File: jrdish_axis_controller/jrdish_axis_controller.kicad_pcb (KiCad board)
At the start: 4 copper layers, 100 x 100 mm, 234 parts, among them CN1 KF2EDGR-2.54-9P, CN10 KF2EDGR-2.54-2P, CN11 KF2EDGR-2.54-3P, CN12 KF2EDGR-2.54-9P, CN13 KF2EDGR-2.54-6P, CN14 KF2EDGR-2.54-6P, CN2 KF2EDGR-2.54-6P, CN3 KF2EDGR-2.54-4P, CN4 KF2EDGR-2.54-4P, CN5 KF2EDGR-2.54-4P, CN7 SM04B-SRSS-TB (LF)(SN), CN8 SM04B-SRSS-TB (LF)(SN), CN9 KF2EDGR-2.54-2P, J1 Conn_ARM_SWD_TagConnect_TC2030, M1 MountingHole_2.7mm_M2.5_ISO14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, Q1 AO3407A, Q2 AO3400A, Q3 BSS138, Q4 AO3407A, Q5 BSS138, Q6 BSS138, Q7 BSS138, Q8 BSS138, SW1 DSHP04TSGER, SW2 SS-12F49-G050, U1 STM32G474RET6, U2 ISOW1432BDFMR, U3 ISOW1432BDFMR, U4 MP2322GQH-Z, U5 LTC4311ISC6#TRPBF, U6 LM75BIMX-3/NOPB, U7 W25Q32JVSSIQ_C179173, X1 NX2016SA-16MHZ-EXS00A-CS07826

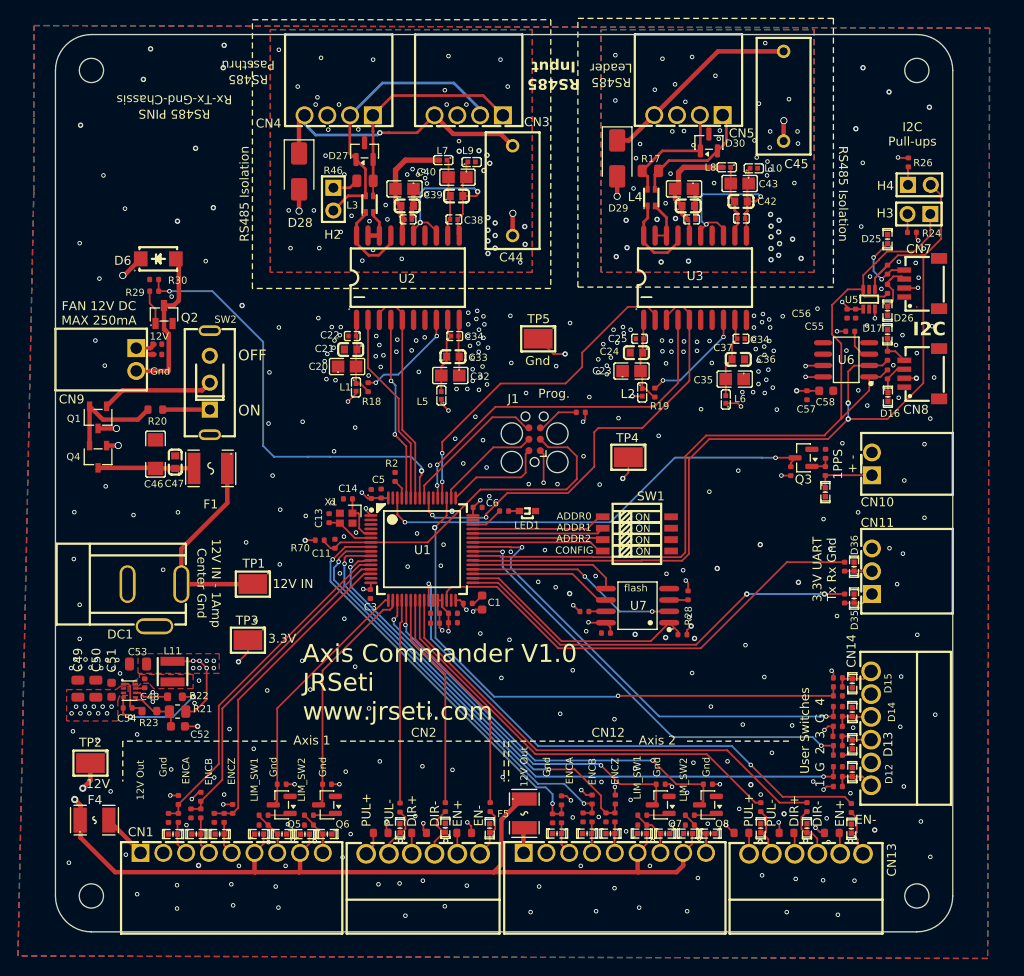
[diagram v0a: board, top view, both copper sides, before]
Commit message: Updates for replacing 10k resistors and encoder RC.
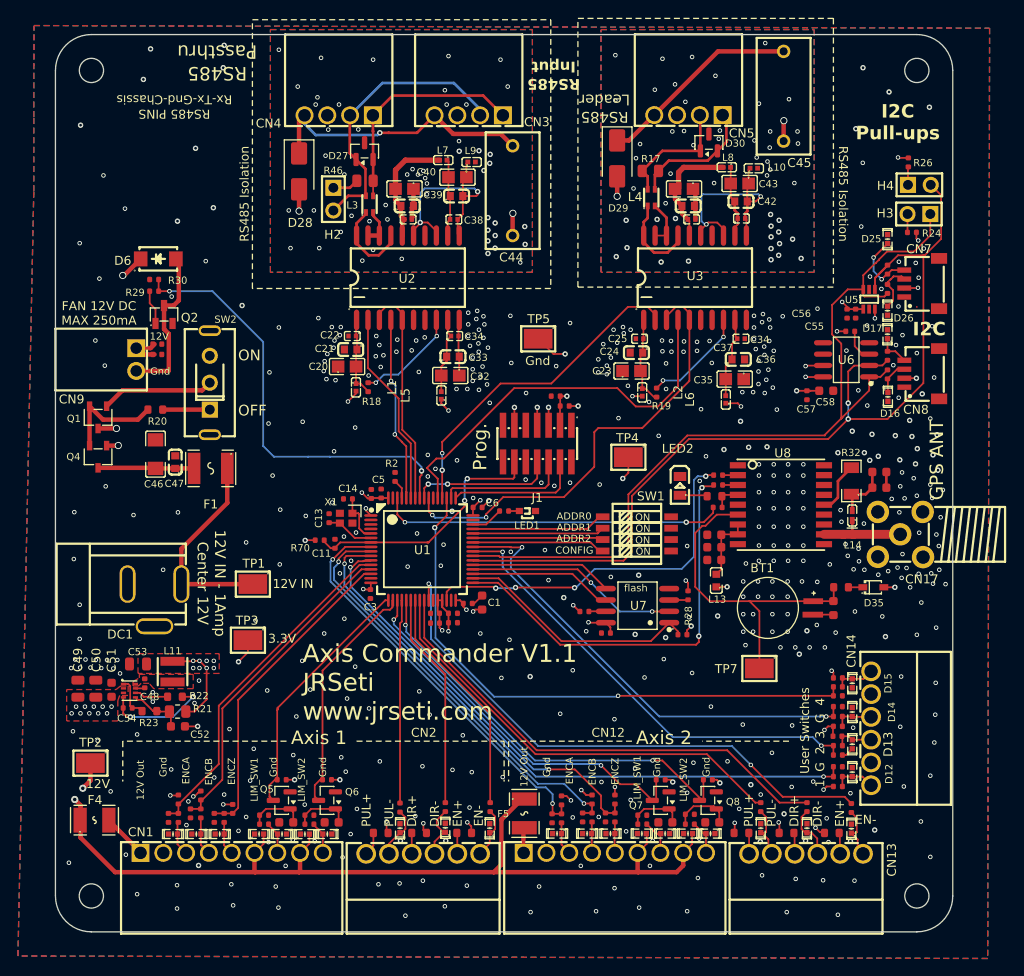
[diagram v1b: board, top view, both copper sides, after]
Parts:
- removed CN10: KF2EDGR-2.54-2P, MyParts:CONN-TH_P2.54_KF2EDGR-2.54-2P
- removed CN11: KF2EDGR-2.54-3P, MyParts:CONN-TH_3P-P2.54_KF2EDGR-2.54-3P
- removed D24, D36: TPESD0402G05V, MyParts:D0402-BI
- removed Q3: BSS138, Package_TO_SOT_SMD:SOT-23
- removed R63: 10kΩ, PCM_JLCPCB:R_0402
- added BT1: MS621FE-FL11E, MyParts:BAT_MS621FE-FL11E, F.Cu at (194.8, 96.5)
- added C12: 10nF, PCM_JLCPCB:C_0603, F.Cu at (207.2, 81.3)
- added C18: 100nF, PCM_JLCPCB:C_0402, F.Cu at (171.2, 72.9)
- added C19: 10uF, PCM_JLCPCB:C_0603, F.Cu at (188.8, 91.2)
- added C62: 100nF, PCM_JLCPCB:C_0603, F.Cu at (188.8, 89.7)
- added C63: 1uF, PCM_JLCPCB:C_0603, F.Cu at (202.1, 96.5)
- added C64: 100nF, PCM_JLCPCB:C_0603, F.Cu at (188.8, 88.3)
- added C65: 47pF, PCM_JLCPCB:C_0603, F.Cu at (207.2, 83.1)
- added C66: 10nF, PCM_JLCPCB:C_0603, F.Cu at (141.1, 120.4)
- added C70: 10nF, PCM_JLCPCB:C_0603, F.Cu at (146.2, 120.4)
- added C71: 10nF, PCM_JLCPCB:C_0603, F.Cu at (183.4, 120.4)
- added C76: 10nF, PCM_JLCPCB:C_0603, F.Cu at (188.6, 120.4)
- added CN17: SMA-KWE_C7498154, MyParts:SMA-TH_SMA-KWE_C7498154, F.Cu at (209.6, 88.3)
- added L13: BLM18AG601SN1D, MyParts:L0603, F.Cu at (189.1, 93.5)
- added L14: LQG15HS27NJ02D, MyParts:L0402-RD, F.Cu at (204.2, 86.2)
- added LED2: XL-0805QBC, MyParts:LED0805-R-RD, F.Cu at (185.0, 82.9)
- added R1: 1kΩ, PCM_JLCPCB:R_0402, F.Cu at (189.2, 85.3)
- added R12: 1kΩ, PCM_JLCPCB:R_0603, F.Cu at (188.8, 84.0)
- added TP7: RH-5016, MyParts:TESTPOINT-SMD_L3.0-W2.0, F.Cu at (193.8, 103.2)
- added U8: MAX-M10S-00B, MyParts:SMD-18_L10.1-W9.7-P1.10-TL_SKG09F, F.Cu at (196.2, 85.0)
- C15, C16, C17, C67, C68, C69: value 100nF -> 1nF
- D35: value TPESD0402G05V -> 1N4148WS T4; footprint MyParts:D0402-BI -> MyParts:SOD-323_L1.8-W1.3-LS2.5-RD
- J1: value Conn_ARM_SWD_TagConnect_TC2030 -> Conn_ST_STDC14; footprint Connector:Tag-Connect_TC2030-IDC-FP_2x03_P1.27mm_Vertical -> MyParts:HDR-SMD_14P-P1.27_FTSH-107-01-L-DV-K
- R31: footprint PCM_JLCPCB:R_0402 -> PCM_JLCPCB:R_0603
- R32: value 100Ω -> 10Ω; footprint PCM_JLCPCB:R_0402 -> MyParts:R1206
- R33, R34, R35, R4, R5, R6: value 4.7kΩ -> 1kΩ
- R71, R74, R77, R80: value 100kΩ -> 15kΩ
- moved R10 18.9 mm to (189.2, 82.8), turned to 0 degrees
- moved R11 17.4 mm to (189.2, 81.7), turned to 0 degrees
- moved R31 14.1 mm to (202.9, 94.2), turned to 180 degrees
- moved R32 3.10 mm to (204.1, 82.3)
- moved D35 2.49 mm to (206.6, 94.2), turned to 0 degrees
- moved C12 1.93 mm to (172.2, 74.0), turned to 0 degrees
- moved R80 1.20 mm to (186.1, 119.5), turned to 0 degrees
- moved R71 1.10 mm to (138.7, 119.6), turned to 0 degrees
- moved R74 1.10 mm to (143.7, 119.6), turned to 0 degrees
- moved R77 1.10 mm to (180.8, 119.6), turned to 0 degrees
- moved R72 1.00 mm to (138.7, 120.6), turned to 0 degrees
- moved R75 1.00 mm to (143.7, 120.6), turned to 0 degrees
- moved R78 1.00 mm to (180.8, 120.6), turned to 0 degrees
- moved R81 1.00 mm to (186.1, 120.6), turned to 0 degrees
- moved J1 0.57 mm to (169.1, 78.2), turned to 180 degrees
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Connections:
- D35 pad 2: GND -> 3V3
- J1 pad 1: 3V3 -> unconnected-(J1-NC-Pad1)
- J1 pad 2: /SWDIO -> unconnected-(J1-NC-Pad2)
- J1 pad 3: /NRST -> 3V3
- J1 pad 4: /SWCLK -> /SWDIO
- J1 pad 6: /SWO -> /SWCLK
- R10 pad 2: Net-(D35-K) -> Net-(U8-RXD)
- R31 pad 1: 3V3 -> Net-(D35-K)
- R31 pad 2: 1PPS_MCU -> /GPS/V_BCKP
- R32 pad 2: Net-(Q3-G) -> /GPS/VCC_RF
- R33 pad 1: ENC2_A_MCU -> 3V3
- R33 pad 2: 3V3 -> ENC2_A_MCU
- R34 pad 1: ENC2_B_MCU -> 3V3
- R34 pad 2: 3V3 -> ENC2_B_MCU
- R35 pad 1: ENC2_Z_MCU -> 3V3
- R35 pad 2: 3V3 -> ENC2_Z_MCU
- R4 pad 1: ENC1_A_MCU -> 3V3
- R4 pad 2: 3V3 -> ENC1_A_MCU
- R5 pad 1: ENC1_B_MCU -> 3V3
- R5 pad 2: 3V3 -> ENC1_B_MCU
- R6 pad 1: ENC1_Z_MCU -> 3V3
- R6 pad 2: 3V3 -> ENC1_Z_MCU
- R71 pad 1: /Axis Control - 1/LIM1_SW1_RETURN -> Net-(Q5-G)
- R74 pad 1: /Axis Control - 1/LIM1_SW2_RETURN -> Net-(Q6-G)
- R77 pad 1: /Axis Control - 2/LIM2_SW1_RETURN -> Net-(Q7-G)
- R80 pad 1: /Axis Control - 2/LIM2_SW2_RETURN -> Net-(Q8-G)
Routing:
- net /GPS/V_BCKP: track 0.00 -> 37.2 mm
- net 1PPS_MCU: track 50.9 -> 38.4 mm
- net RS232_RX_MCU: track 52.3 -> 41.5 mm, vias 0 -> 4
- net /NRST: track 39.3 -> 28.5 mm, vias 0 -> 2
- net /GPS/RF_IN: track 0.00 -> 10.1 mm
- net GND: track 23.5 -> 31.6 mm, vias 338 -> 465
- net Net-(U8-VCC): track 0.00 -> 7.60 mm
- net /GPS/VCC_RF: track 0.00 -> 5.83 mm
- net Net-(Q8-G): track 2.53 -> 6.68 mm
- net Net-(Q7-G): track 2.57 -> 6.43 mm
- net Net-(Q6-G): track 2.53 -> 6.34 mm
- net Net-(Q5-G): track 2.53 -> 6.33 mm
- net /SWDIO: track 11.6 -> 15.0 mm
- net RS485_2_RX_MCU: track 41.4 -> 44.7 mm, vias 2 -> 0
- net /GPS/TIMEPULSE: track 0.00 -> 3.11 mm
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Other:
- board text added: "12V IN - 1Amp Center 12V"
- board text added: "Axis Commander V1.1 JRSeti www.jrseti.com"
- board text added: "GPS ANT"
- board text removed: "12V IN - 1Amp Center Gnd"
- board text removed: "1PPS + -"
- board text removed: "3.3V UART Tx Rx Gnd"
- board text removed: "Axis Commander V1.0 JRSeti www.jrseti.com"
